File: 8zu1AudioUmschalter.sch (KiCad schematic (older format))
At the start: 56 parts, among them IC1 ATMEGA8A-A, IC2 MAX9890, J1 USB, J2 LUM 1503-07, J3 LUM 1503-07, J4 LUM 1503-07, J5 LUM 1503-07, J6 LUM 1503-07, J7 LUM 1503-07, J8 LUM 1503-07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

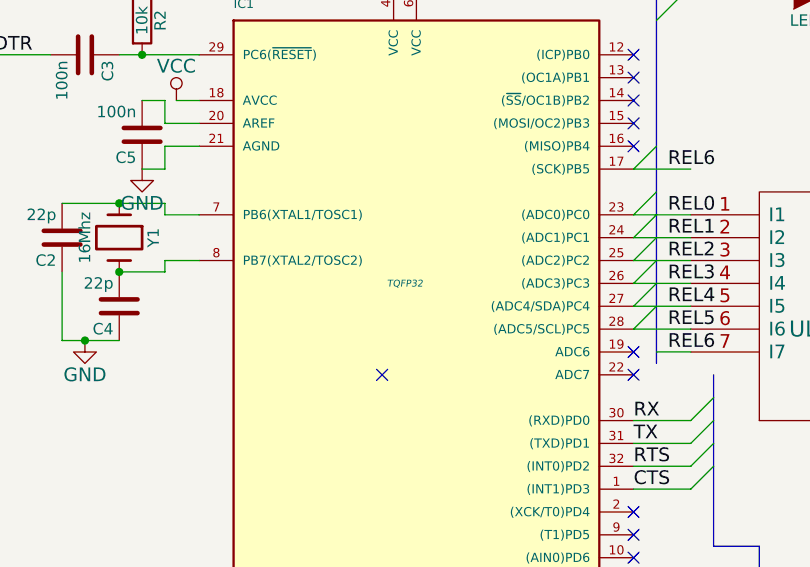
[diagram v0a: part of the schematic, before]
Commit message: footprints für buchse und relais schauen ok aus, bauteile weiter zugeordnet
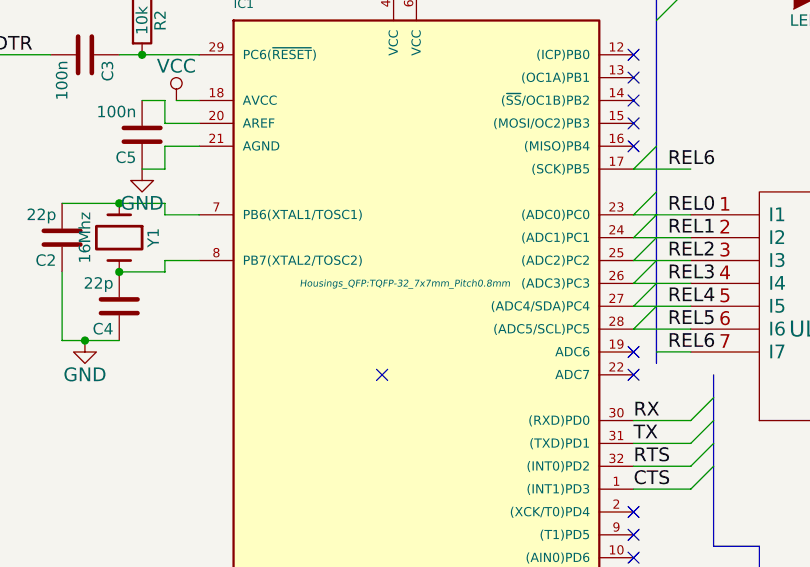
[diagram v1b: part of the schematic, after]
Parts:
- 100n1, C10, C11, C12, C2, C3, C4, C5, C6, C7, C9: footprint (none) -> Capacitors_SMD:C_0603
- C1, C8: footprint (none) -> Capacitors_SMD:C_0805
- D1, D10, D2, D3, D4, D5, D6, D7, D8, D9: footprint (none) -> LEDs:LED-0603
- IC1: footprint TQFP32 -> Housings_QFP:TQFP-32_7x7mm_Pitch0.8mm
- J1: footprint (none) -> Connect:USB_Mini-B
- R1, R10, R11, R12, R2, R3, R4, R5, R6, R7, R8, R9: footprint (none) -> Resistors_SMD:R_0603_HandSoldering

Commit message: Aktualisierung der Footprintzuordnung, Erstellen von TDFN8
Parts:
- J2, J3, J4, J5, J6, J7, J8, J9: footprint (none) -> Audio3:LUM1503
- K1, K2, K3, K4, K5, K6, K7: footprint (none) -> Audio3:REL_NA05W
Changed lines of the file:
@@
-$EndComp
-$Comp
-L FT232RL U1
-U 1 1 550493C1
-P 7450 8950
-F 0 "U1" H 6700 10150 60  0000 C CNN
-F 1 "FT232RL" H 7450 8950 60  0000 C CNN
-F 2 "" H 7450 8950 60  0001 C CNN
-F 3 "" H 7450 8950 60  0000 C CNN
-	1    7450 8950
-	1    0    0    -1
 $EndComp
 $Comp
@@
 F 0 "J2" H 5950 6850 50  0000 C CNN
 F 1 "LUM 1503-07" H 6150 7300 50  0000 C CNN
-F 2 "" H 6300 7050 60  0001 C CNN
+F 2 "Audio3:LUM1503" H 6300 7050 60  0001 C CNN
 F 3 "" H 6300 7050 60  0000 C CNN
 	1    6300 7050
@@
 F 0 "J8" H 14500 1150 50  0000 C CNN
 F 1 "LUM 1503-07" H 14700 1600 50  0000 C CNN
-F 2 "" H 14850 1350 60  0001 C CNN
+F 2 "Audio3:LUM1503" H 14850 1350 60  0001 C CNN
 F 3 "" H 14850 1350 60  0000 C CNN
 	1    14850 1350
@@
 F 0 "J9" H 14500 2250 50  0000 C CNN
 F 1 "LUM 1503-07" H 14700 2700 50  0000 C CNN
-F 2 "" H 14850 2450 60  0001 C CNN
+F 2 "Audio3:LUM1503" H 14850 2450 60  0001 C CNN
 F 3 "" H 14850 2450 60  0000 C CNN
 	1    14850 2450
@@
 F 0 "J6" H 14450 3350 50  0000 C CNN
 F 1 "LUM 1503-07" H 14650 3800 50  0000 C CNN
-F 2 "" H 14800 3550 60  0001 C CNN
+F 2 "Audio3:LUM1503" H 14800 3550 60  0001 C CNN
 F 3 "" H 14800 3550 60  0000 C CNN
 	1    14800 3550
@@
 F 0 "J7" H 14450 4400 50  0000 C CNN
 F 1 "LUM 1503-07" H 14650 4850 50  0000 C CNN
-F 2 "" H 14800 4600 60  0001 C CNN
+F 2 "Audio3:LUM1503" H 14800 4600 60  0001 C CNN
 F 3 "" H 14800 4600 60  0000 C CNN
 	1    14800 4600
@@
 F 0 "K1" H 10800 1850 50  0000 C CNN
 F 1 "RELAY_2RT" H 11000 950 50  0000 C CNN
-F 2 "" H 10850 1450 60  0001 C CNN
+F 2 "Audio3:REL_NA05W" H 10850 1450 60  0001 C CNN
 F 3 "" H 10850 1450 60  0000 C CNN
 	1    10850 1450
@@
 F 0 "J3" H 11700 1100 50  0000 C CNN
 F 1 "LUM 1503-07" H 11900 1550 50  0000 C CNN
-F 2 "" H 12050 1300 60  0001 C CNN
+F 2 "Audio3:LUM1503" H 12050 1300 60  0001 C CNN
 F 3 "" H 12050 1300 60  0000 C CNN
 	1    12050 1300
@@
 F 0 "K2" H 10800 3000 50  0000 C CNN
 F 1 "RELAY_2RT" H 11000 2100 50  0000 C CNN
-F 2 "" H 10850 2600 60  0001 C CNN
+F 2 "Audio3:REL_NA05W" H 10850 2600 60  0001 C CNN
 F 3 "" H 10850 2600 60  0000 C CNN
 	1    10850 2600
@@
 F 0 "J4" H 11700 2250 50  0000 C CNN
 F 1 "LUM 1503-07" H 11900 2700 50  0000 C CNN
-F 2 "" H 12050 2450 60  0001 C CNN
+F 2 "Audio3:LUM1503" H 12050 2450 60  0001 C CNN
 F 3 "" H 12050 2450 60  0000 C CNN
 	1    12050 2450
@@
 F 0 "K3" H 10850 4100 50  0000 C CNN
 F 1 "RELAY_2RT" H 11050 3200 50  0000 C CNN
-F 2 "" H 10900 3700 60  0001 C CNN
+F 2 "Audio3:REL_NA05W" H 10900 3700 60  0001 C CNN
 F 3 "" H 10900 3700 60  0000 C CNN
 	1    10900 3700
@@
 F 0 "J5" H 11750 3350 50  0000 C CNN
 F 1 "LUM 1503-07" H 11950 3800 50  0000 C CNN
-F 2 "" H 12100 3550 60  0001 C CNN
+F 2 "Audio3:LUM1503" H 12100 3550 60  0001 C CNN
 F 3 "" H 12100 3550 60  0000 C CNN
 	1    12100 3550
@@
 F 0 "K6" H 13600 1900 50  0000 C CNN
 F 1 "RELAY_2RT" H 13800 1000 50  0000 C CNN
-F 2 "" H 13650 1500 60  0001 C CNN
+F 2 "Audio3:REL_NA05W" H 13650 1500 60  0001 C CNN
 F 3 "" H 13650 1500 60  0000 C CNN
 	1    13650 1500
@@
 F 0 "K7" H 13600 3000 50  0000 C CNN
 F 1 "RELAY_2RT" H 13800 2100 50  0000 C CNN
-F 2 "" H 13650 2600 60  0001 C CNN
+F 2 "Audio3:REL_NA05W" H 13650 2600 60  0001 C CNN
 F 3 "" H 13650 2600 60  0000 C CNN
 	1    13650 2600
@@
 F 0 "K4" H 13550 4100 50  0000 C CNN
 F 1 "RELAY_2RT" H 13750 3200 50  0000 C CNN
-F 2 "" H 13600 3700 60  0001 C CNN
+F 2 "Audio3:REL_NA05W" H 13600 3700 60  0001 C CNN
 F 3 "" H 13600 3700 60  0000 C CNN
 	1    13600 3700
@@
 F 0 "K5" H 13550 5150 50  0000 C CNN
 F 1 "RELAY_2RT" H 13750 4250 50  0000 C CNN
-F 2 "" H 13600 4750 60  0001 C CNN
+F 2 "Audio3:REL_NA05W" H 13600 4750 60  0001 C CNN
 F 3 "" H 13600 4750 60  0000 C CNN
 	1    13600 4750
@@
 Entry Wire Line
 	11350 9750 11450 9650
+$Comp
+L FT232RL U1
+U 1 1 550493C1
+P 7450 8950
+F 0 "U1" H 6700 10150 60  0000 C CNN
+F 1 "FT232RL" H 7450 8950 60  0000 C CNN
+F 2 "" H 7450 8950 60  0001 C CNN
+F 3 "" H 7450 8950 60  0000 C CNN
+	1    7450 8950
+	1    0    0    -1
+$EndComp
 $EndSCHEMATC

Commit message: footprints für widerstände und maximchip angepasst
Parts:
- IC2: footprint (none) -> Housings_DFN_QFN:DFN-8-1EP_3x3mm_Pitch0.65mm
- R1, R10, R11, R12, R2, R3, R4, R5, R6, R7, R8, R9: footprint Resistors_SMD:R_0603_HandSoldering -> Resistors_SMD:R_0603
- U1: footprint (none) -> Housings_SSOP:SSOP-28_5.3x10.2mm_Pitch0.65mm
- U2: footprint (none) -> SMD_Packages:SO-16-N
- Y1: footprint (none) -> Crystals:Crystal_HC49-U_Vertical
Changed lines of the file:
@@
 F 0 "U2" H 9150 4800 70  0000 C CNN
 F 1 "ULN2003" H 9150 4600 70  0000 C CNN
-F 2 "" H 9150 4700 60  0001 C CNN
+F 2 "SMD_Packages:SO-16-N" H 9150 4700 60  0001 C CNN
 F 3 "" H 9150 4700 60  0000 C CNN
 	1    9150 4700
@@
 F 0 "IC2" H 7500 6650 60  0000 C CNN
 F 1 "MAX9890" H 7750 6950 60  0000 C CNN
-F 2 "" H 7750 6950 60  0001 C CNN
+F 2 "Housings_DFN_QFN:DFN-8-1EP_3x3mm_Pitch0.65mm" H 7750 6950 60  0001 C CNN
 F 3 "" H 7750 6950 60  0000 C CNN
 	1    7750 6950
@@
 F 0 "R4" V 8880 9250 50  0000 C CNN
 F 1 "270" V 8800 9250 50  0000 C CNN
-F 2 "Resistors_SMD:R_0603_HandSoldering" V 8730 9250 30  0001 C CNN
+F 2 "Resistors_SMD:R_0603" V 8730 9250 30  0001 C CNN
 F 3 "" H 8800 9250 30  0000 C CNN
 	1    8800 9250
@@
 F 0 "R5" V 8880 9400 50  0000 C CNN
 F 1 "270" V 8800 9400 50  0000 C CNN
-F 2 "Resistors_SMD:R_0603_HandSoldering" V 8730 9400 30  0001 C CNN
+F 2 "Resistors_SMD:R_0603" V 8730 9400 30  0001 C CNN
 F 3 "" H 8800 9400 30  0000 C CNN
 	1    8800 9400
@@
 F 0 "R1" V 5880 7750 50  0000 C CNN
 F 1 "270" V 5800 7750 50  0000 C CNN
-F 2 "Resistors_SMD:R_0603_HandSoldering" V 5730 7750 30  0001 C CNN
+F 2 "Resistors_SMD:R_0603" V 5730 7750 30  0001 C CNN
 F 3 "" H 5800 7750 30  0000 C CNN
 	1    5800 7750
@@
 F 0 "R2" V 6180 3450 50  0000 C CNN
 F 1 "10k" V 6100 3450 50  0000 C CNN
-F 2 "Resistors_SMD:R_0603_HandSoldering" V 6030 3450 30  0001 C CNN
+F 2 "Resistors_SMD:R_0603" V 6030 3450 30  0001 C CNN
 F 3 "" H 6100 3450 30  0000 C CNN
 	1    6100 3450
@@
 F 0 "Y1" H 6000 4550 50  0000 C CNN
 F 1 "16Mhz" H 6000 4250 50  0000 C CNN
-F 2 "" H 6000 4400 60  0001 C CNN
+F 2 "Crystals:Crystal_HC49-U_Vertical" H 6000 4400 60  0001 C CNN
 F 3 "" H 6000 4400 60  0000 C CNN
 	1    6000 4400
@@
 F 0 "R6" V 9430 1850 50  0000 C CNN
 F 1 "270" V 9350 1850 50  0000 C CNN
-F 2 "Resistors_SMD:R_0603_HandSoldering" V 9280 1850 30  0001 C CNN
+F 2 "Resistors_SMD:R_0603" V 9280 1850 30  0001 C CNN
 F 3 "" H 9350 1850 30  0000 C CNN
 	1    9350 1850
@@
 F 0 "R7" V 9430 2100 50  0000 C CNN
 F 1 "270" V 9350 2100 50  0000 C CNN
-F 2 "Resistors_SMD:R_0603_HandSoldering" V 9280 2100 30  0001 C CNN
+F 2 "Resistors_SMD:R_0603" V 9280 2100 30  0001 C CNN
 F 3 "" H 9350 2100 30  0000 C CNN
 	1    9350 2100
@@
 F 0 "R8" V 9430 2350 50  0000 C CNN
 F 1 "270" V 9350 2350 50  0000 C CNN
-F 2 "Resistors_SMD:R_0603_HandSoldering" V 9280 2350 30  0001 C CNN
+F 2 "Resistors_SMD:R_0603" V 9280 2350 30  0001 C CNN
 F 3 "" H 9350 2350 30  0000 C CNN
 	1    9350 2350
@@
 F 0 "R9" V 9430 2600 50  0000 C CNN
 F 1 "270" V 9350 2600 50  0000 C CNN
-F 2 "Resistors_SMD:R_0603_HandSoldering" V 9280 2600 30  0001 C CNN
+F 2 "Resistors_SMD:R_0603" V 9280 2600 30  0001 C CNN
 F 3 "" H 9350 2600 30  0000 C CNN
 	1    9350 2600
@@
 F 0 "R10" V 9430 2850 50  0000 C CNN
 F 1 "270" V 9350 2850 50  0000 C CNN
-F 2 "Resistors_SMD:R_0603_HandSoldering" V 9280 2850 30  0001 C CNN
+F 2 "Resistors_SMD:R_0603" V 9280 2850 30  0001 C CNN
 F 3 "" H 9350 2850 30  0000 C CNN
 	1    9350 2850
@@
 F 0 "R11" V 9430 3100 50  0000 C CNN
 F 1 "270" V 9350 3100 50  0000 C CNN
-F 2 "Resistors_SMD:R_0603_HandSoldering" V 9280 3100 30  0001 C CNN
+F 2 "Resistors_SMD:R_0603" V 9280 3100 30  0001 C CNN
 F 3 "" H 9350 3100 30  0000 C CNN
 	1    9350 3100
@@
 F 0 "R12" V 9430 3350 50  0000 C CNN
 F 1 "270" V 9350 3350 50  0000 C CNN
-F 2 "Resistors_SMD:R_0603_HandSoldering" V 9280 3350 30  0001 C CNN
+F 2 "Resistors_SMD:R_0603" V 9280 3350 30  0001 C CNN
 F 3 "" H 9350 3350 30  0000 C CNN
 	1    9350 3350
@@
 F 0 "R3" V 8530 6400 50  0000 C CNN
 F 1 "47k" V 8450 6400 50  0000 C CNN
-F 2 "Resistors_SMD:R_0603_HandSoldering" V 8380 6400 30  0001 C CNN
+F 2 "Resistors_SMD:R_0603" V 8380 6400 30  0001 C CNN
 F 3 "" H 8450 6400 30  0000 C CNN
 	1    8450 6400
@@
 F 0 "U1" H 6700 10150 60  0000 C CNN
 F 1 "FT232RL" H 7450 8950 60  0000 C CNN
-F 2 "" H 7450 8950 60  0001 C CNN
+F 2 "Housings_SSOP:SSOP-28_5.3x10.2mm_Pitch0.65mm" H 7450 8950 60  0001 C CNN
 F 3 "" H 7450 8950 60  0000 C CNN
 	1    7450 8950

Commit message: Erster PCB Entwurf
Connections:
- net REL0: now also IC1.28 ((ADC5/SCL)PC5); no longer IC1.23 ((ADC0)PC0)
- net REL1: now also IC1.27 ((ADC4/SDA)PC4); no longer IC1.24 ((ADC1)PC1)
- net REL2: now also IC1.26 ((ADC3)PC3); no longer IC1.25 ((ADC2)PC2)
- net REL3: now also IC1.25 ((ADC2)PC2); no longer IC1.26 ((ADC3)PC3)
- net REL4: now also IC1.24 ((ADC1)PC1); no longer IC1.27 ((ADC4/SDA)PC4)
- net REL5: now also IC1.23 ((ADC0)PC0); no longer IC1.28 ((ADC5/SCL)PC5)
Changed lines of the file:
@@
 	10350 4900 9800 4900
-Wire Wire Line
-	8250 4300 8500 4300
-Wire Wire Line
-	8250 4400 8500 4400
-Wire Wire Line
-	8250 4500 8500 4500
-Wire Wire Line
-	8250 4600 8500 4600
-Wire Wire Line
-	8250 4700 8500 4700
-Wire Wire Line
-	8250 4800 8500 4800
 Wire Wire Line
 	8300 6750 8250 6750
@@
 Wire Bus Line
 	8350 1700 8350 4950
-Text Label 8400 4300 0    60   ~ 0
+Text Label 8500 4300 0    60   ~ 0
 REL0
-Text Label 8400 4400 0    60   ~ 0
+Text Label 8500 4400 0    60   ~ 0
 REL1
-Text Label 8400 4500 0    60   ~ 0
+Text Label 8500 4500 0    60   ~ 0
 REL2
-Text Label 8400 4600 0    60   ~ 0
+Text Label 8500 4600 0    60   ~ 0
 REL3
-Text Label 8400 4700 0    60   ~ 0
+Text Label 8500 4700 0    60   ~ 0
 REL4
-Text Label 8400 4800 0    60   ~ 0
+Text Label 8500 4800 0    60   ~ 0
 REL5
-Text Label 8400 4900 0    60   ~ 0
+Text Label 8500 4900 0    60   ~ 0
 REL6
 Entry Wire Line
@@
 	1    0    0    -1
 $EndComp
+Text Label 8250 4300 0    60   ~ 0
+REL5
+Text Label 8250 4400 0    60   ~ 0
+REL4
+Text Label 8250 4500 0    60   ~ 0
+REL3
+Text Label 8250 4600 0    60   ~ 0
+REL2
+Text Label 8250 4700 0    60   ~ 0
+REL1
+Text Label 8250 4800 0    60   ~ 0
+REL0
 $EndSCHEMATC
